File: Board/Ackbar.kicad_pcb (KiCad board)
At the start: 2 copper layers, 101.6 x 50.8 mm, 13 parts, among them J1 TOF, J2 GNSS, J3 HALL, J4 MOTOR, J5 PWR_IN, J6 EPD, U1 ESP32-S3 Pico, U2 VREG, U3 TMC2209

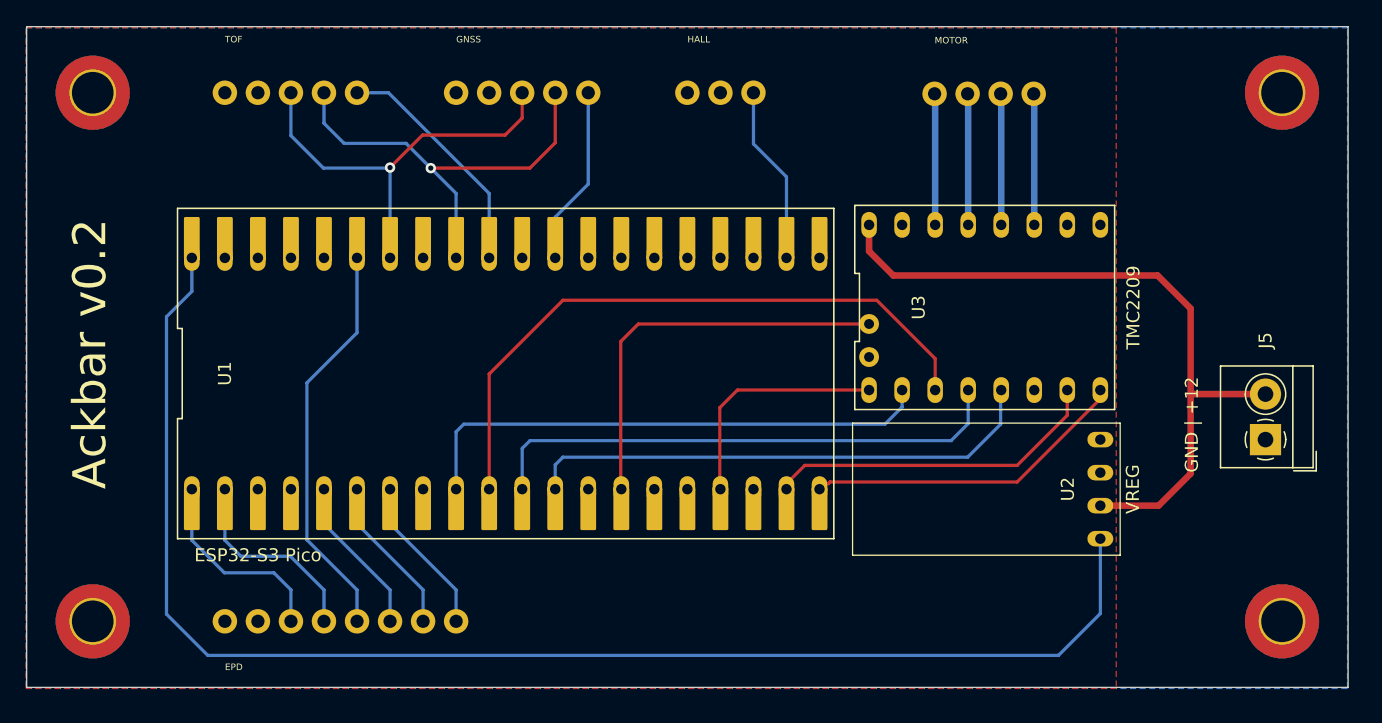
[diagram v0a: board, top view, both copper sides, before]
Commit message: add inverter to schematic
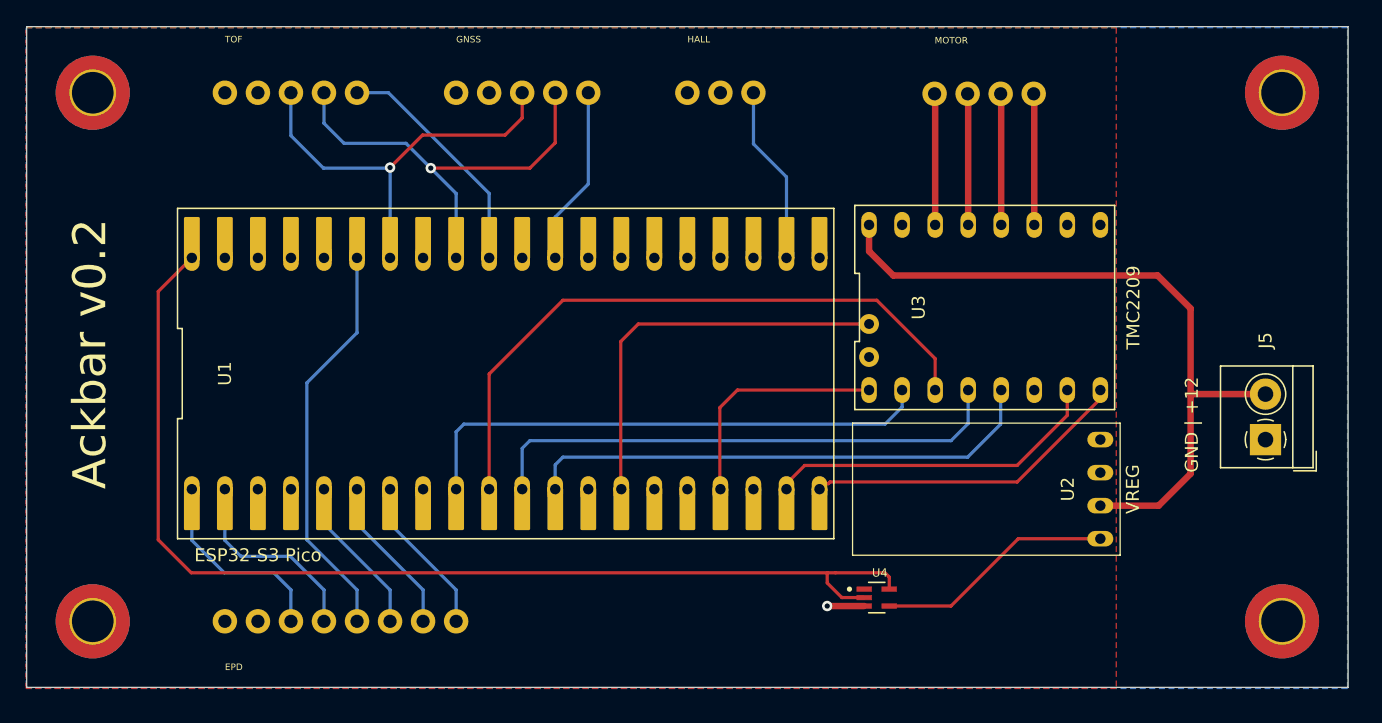
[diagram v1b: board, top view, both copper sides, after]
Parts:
- added U4: SN74LVC1G04DCKR, Ackbar:SOT65P210X110-5N, F.Cu at (77.5, 55.9)
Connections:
- U1 pad 40: /VBUS -> Net-(U1-VBUS)
- U2 pad 4: /VBUS -> Net-(U2-EN)
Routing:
- net /VBUS: track 108.4 -> 0.00 mm
- net Net-(U1-VBUS): track 0.00 -> 85.2 mm
- net Net-(U2-EN): track 0.00 -> 18.4 mm
- net /GND: track 0.00 -> 2.85 mm, vias 0 -> 1
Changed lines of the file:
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@@
   (net 15 "unconnected-(U1-GP36-Pad15)")
   (net 16 "unconnected-(U1-GP37-Pad16)")
-  (net 17 "/VBUS")
+  (net 17 "Net-(U1-VBUS)")
   (net 18 "/STP_EN")
   (net 19 "/STP_CLK")
@@
   (net 39 "/M_B1")
   (net 40 "/M_B2")
+  (net 41 "Net-(U2-EN)")
   (footprint "Ackbar:Waveshare ESP32-S3 Pico" (layer "F.Cu")
     (at 48.938 38.654334)
@@
       ))
     (pad "40" thru_hole custom (at -24.13 -8.89) (size 1.2 2) (drill 0.8) (layers "*.Cu" "*.Mask")
-      (net 17 "/VBUS") (pinfunction "VBUS") (pintype "power_in") (thermal_bridge_angle 45)
+      (net 17 "Net-(U1-VBUS)") (pinfunction "VBUS") (pintype "power_in") (thermal_bridge_angle 45)
       (options (clearance outline) (anchor circle))
       (primitives
@@
         (gr_rect (start -0.508 -3.048) (end 0.508 0) (width 0.2) (fill yes))
       ))
+  )
+  (footprint "Ackbar:SOT65P210X110-5N" (layer "F.Cu")
+    (at 77.47 55.88)
+    (property "Check_prices" "https://www.snapeda.com/parts/SN74LVC1G04DCKR/Texas+Instruments/view-part/?ref=eda")
+    (property "Description" "\nSingle 1.65-V to 5.5-V inverter\n")
+    (property "DigiKey_Part_Number" "296-11600-2-ND")
+    (property "MF" "Texas Instruments")
+    (property "MP" "SN74LVC1G04DCKR")
+    (property "Package" "SC70-5 Texas Instruments")
+    (property "Purchase-URL" "https://www.snapeda.com/api/url_track_click_mouser/?unipart_id=359755&manufacturer=Texas Instruments&part_name=SN74LVC1G04DCKR&search_term=None")
+    (property "Sheetfile" "Ackbar.kicad_sch")
+    (property "Sheetname" "")
+    (property "SnapEDA_Link" "https://www.snapeda.com/parts/SN74LVC1G04DCKR/Texas+Instruments/view-part/?ref=snap")
+    (attr smd)
+    (fp_text reference "U4" (at 0.232 -1.9064) (layer "F.SilkS")
+        (effects (font (size 0.64 0.64) (thickness 0.15)))
+    )
+    (fp_text value "SN74LVC1G04DCKR" (at 4.7024 1.9064) (layer "F.Fab")
+        (effects (font (size 0.64 0.64) (thickness 0.15)))
+    )
+    (fp_line (start -0.625 -1.17) (end 0.625 -1.17)
+      (stroke (width 0.127) (type solid)) (layer "F.SilkS"))
+    (fp_line (start 0.625 1.17) (end -0.625 1.17)
+      (stroke (width 0.127) (type solid)) (layer "F.SilkS"))
+    (fp_circle (center -2.1 -0.65) (end -2 -0.65)
+      (stroke (width 0.2) (type solid)) (fill none) (layer "F.SilkS"))
+    (fp_line (start -1.81 -1.33) (end 1.81 -1.33)
+      (stroke (width 0.05) (type solid)) (layer "F.CrtYd"))
+    (fp_line (start -1.81 1.33) (end -1.81 -1.33)
+      (stroke (width 0.05) (type solid)) (layer "F.CrtYd"))
+    (fp_line (start 1.81 -1.33) (end 1.81 1.33)
+      (stroke (width 0.05) (type solid)) (layer "F.CrtYd"))
+    (fp_line (start 1.81 1.33) (end -1.81 1.33)
+      (stroke (width 0.05) (type solid)) (layer "F.CrtYd"))
+    (fp_line (start -0.625 -1) (end 0.625 -1)
+      (stroke (width 0.127) (type solid)) (layer "F.Fab"))
+    (fp_line (start -0.625 1) (end -0.625 -1)
+      (stroke (width 0.127) (type solid)) (layer "F.Fab"))
+    (fp_line (start 0.625 -1) (end 0.625 1)
+      (stroke (width 0.127) (type solid)) (layer "F.Fab"))
+    (fp_line (start 0.625 1) (end -0.625 1)
+      (stroke (width 0.127) (type solid)) (layer "F.Fab"))
+    (fp_circle (center -2.1 -0.65) (end -2 -0.65)
+      (stroke (width 0.2) (type solid)) (fill none) (layer "F.Fab"))
+    (pad "1" smd roundrect (at -0.96 -0.65) (size 1.19 0.4) (layers "F.Cu" "F.Paste" "F.Mask") (roundrect_rratio 0.05)
+      (solder_mask_margin 0.102))
+    (pad "2" smd roundrect (at -0.96 0) (size 1.19 0.4) (layers "F.Cu" "F.Paste" "F.Mask") (roundrect_rratio 0.05)
+      (net 17 "Net-(U1-VBUS)") (pinfunction "A") (pintype "input") (solder_mask_margin 0.102))
+    (pad "3" smd roundrect (at -0.96 0.65) (size 1.19 0.4) (layers "F.Cu" "F.Paste" "F.Mask") (roundrect_rratio 0.05)
+      (net 9 "/GND") (pinfunction "GND") (pintype "power_in") (solder_mask_margin 0.102))
+    (pad "4" smd roundrect (at 0.96 0.65) (size 1.19 0.4) (layers "F.Cu" "F.Paste" "F.Mask") (roundrect_rratio 0.05)
+      (net 41 "Net-(U2-EN)") (pinfunction "Y") (pintype "output") (solder_mask_margin 0.102))
+    (pad "5" smd roundrect (at 0.96 -0.65) (size 1.19 0.4) (layers "F.Cu" "F.Paste" "F.Mask") (roundrect_rratio 0.05)
+      (net 17 "Net-(U1-VBUS)") (pinfunction "VCC") (pintype "power_in") (solder_mask_margin 0.102))
   )
   (footprint "MountingHole:MountingHole_3.2mm_M3_ISO7380_Pad_TopBottom" (layer "F.Cu")
@@
       (net 11 "/VIN") (pinfunction "VIN") (pintype "power_in") (thermal_bridge_angle 45))
     (pad "4" thru_hole oval (at 0 -3.81 270) (size 1.2 2) (drill 0.8) (layers "*.Cu" "*.Mask")
-      (net 17 "/VBUS") (pinfunction "EN") (pintype "input") (thermal_bridge_angle 45))
+      (net 41 "Net-(U2-EN)") (pinfunction "EN") (pintype "input") (thermal_bridge_angle 45))
   )
   (footprint "MountingHole:MountingHole_3.2mm_M3_ISO7380_Pad_TopBottom" (layer "F.Cu")
@@
     (effects (font (size 2.54 2.54) (thickness 0.15)) (justify left bottom))
   )
+  (segment (start 73.66 56.53) (end 76.51 56.53) (width 0.5) (layer "F.Cu") (net 9))
+  (via (at 73.66 56.53) (size 0.8) (drill 0.4) (layers "F.Cu" "B.Cu") (net 9))
   (segment (start 99.06 31.115) (end 78.74 31.115) (width 0.5) (layer "F.Cu") (net 11))
   (segment (start 78.74 31.115) (end 76.878 29.253) (width 0.5) (layer "F.Cu") (net 11))
@@
   (segment (start 67.988 20.998) (end 67.988 17.064334) (width 0.25) (layer "B.Cu") (net 14))
   (segment (start 70.528 29.764334) (end 70.528 23.538) (width 0.25) (layer "B.Cu") (net 14))
-  (segment (start 24.808 29.764334) (end 24.808 32.342) (width 0.25) (layer "B.Cu") (net 17))
-  (segment (start 91.44 60.325) (end 94.658 57.107) (width 0.25) (layer "B.Cu") (net 17))
-  (segment (start 22.86 57.15) (end 26.035 60.325) (width 0.25) (layer "B.Cu") (net 17))
-  (segment (start 26.035 60.325) (end 91.44 60.325) (width 0.25) (layer "B.Cu") (net 17))
-  (segment (start 94.658 57.107) (end 94.658 51.354334) (width 0.25) (layer "B.Cu") (net 17))
-  (segment (start 24.808 32.342) (end 22.86 34.29) (width 0.25) (layer "B.Cu") (net 17))
-  (segment (start 22.86 34.29) (end 22.86 57.15) (width 0.25) (layer "B.Cu") (net 17))
+  (segment (start 78.43 54.3) (end 78.105 53.975) (width 0.25) (layer "F.Cu") (net 17))
+  (segment (start 22.225 51.435) (end 22.225 32.347334) (width 0.25) (layer "F.Cu") (net 17))
+  (segment (start 22.225 32.347334) (end 24.808 29.764334) (width 0.25) (layer "F.Cu") (net 17))
+  (segment (start 78.43 55.23) (end 78.43 54.3) (width 0.25) (layer "F.Cu") (net 17))
+  (segment (start 73.66 54.751452) (end 74.788548 55.88) (width 0.25) (layer "F.Cu") (net 17))
+  (segment (start 24.765 53.975) (end 22.225 51.435) (width 0.25) (layer "F.Cu") (net 17))
+  (segment (start 74.295 53.975) (end 24.765 53.975) (width 0.25) (layer "F.Cu") (net 17))
+  (segment (start 73.66 53.975) (end 73.66 54.751452) (width 0.25) (layer "F.Cu") (net 17))
+  (segment (start 78.105 53.975) (end 74.295 53.975) (width 0.25) (layer "F.Cu") (net 17))
+  (segment (start 74.788548 55.88) (end 76.51 55.88) (width 0.25) (layer "F.Cu") (net 17))
   (segment (start 65.405 47.119334) (end 65.448 47.119334) (width 0.25) (layer "F.Cu") (net 18))
   (segment (start 65.405 41.275) (end 65.405 47.119334) (width 0.25) (layer "F.Cu") (net 18))
@@
   (segment (start 88.265 46.99) (end 73.881375 46.99) (width 0.25) (layer "F.Cu") (net 36))
   (segment (start 73.752041 47.119334) (end 73.068 47.119334) (width 0.25) (layer "F.Cu") (net 36))
+  (segment (start 81.958 27.224334) (end 81.958 17.188) (width 0.5) (layer "F.Cu") (net 37))
   (segment (start 81.958 17.188) (end 81.915 17.145) (width 0.5) (layer "B.Cu") (net 37))
-  (segment (start 81.958 27.224334) (end 81.958 17.188) (width 0.5) (layer "B.Cu") (net 37))
-  (segment (start 84.498 27.224334) (end 84.498 17.188) (width 0.5) (layer "B.Cu") (net 38))
+  (segment (start 84.498 27.224334) (end 84.498 17.188) (width 0.5) (layer "F.Cu") (net 38))
   (segment (start 84.498 17.188) (end 84.455 17.145) (width 0.5) (layer "B.Cu") (net 38))
-  (segment (start 87.038 27.224334) (end 87.038 17.188) (width 0.5) (layer "B.Cu") (net 39))
+  (segment (start 87.038 27.224334) (end 87.038 17.188) (width 0.5) (layer "F.Cu") (net 39))
   (segment (start 87.038 17.188) (end 86.995 17.145) (width 0.5) (layer "B.Cu") (net 39))
-  (segment (start 89.578 27.224334) (end 89.578 17.188) (width 0.5) (layer "B.Cu") (net 40))
+  (segment (start 89.578 27.224334) (end 89.578 17.188) (width 0.5) (layer "F.Cu") (net 40))
   (segment (start 89.578 17.188) (end 89.535 17.145) (width 0.5) (layer "B.Cu") (net 40))
+  (segment (start 83.17 56.53) (end 88.345666 51.354334) (width 0.25) (layer "F.Cu") (net 41))
+  (segment (start 78.43 56.53) (end 83.17 56.53) (width 0.25) (layer "F.Cu") (net 41))
+  (segment (start 88.345666 51.354334) (end 94.658 51.354334) (width 0.25) (layer "F.Cu") (net 41))
   (zone (net 10) (net_name "/3V3") (layer "F.Cu") (hatch edge 0.5)
     (priority 1)
